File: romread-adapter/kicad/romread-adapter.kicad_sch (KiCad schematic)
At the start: 27 parts

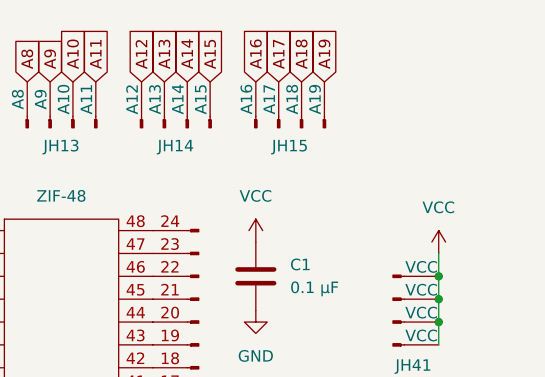
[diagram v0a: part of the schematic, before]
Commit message: romread-adapter sch pcb: Add C2
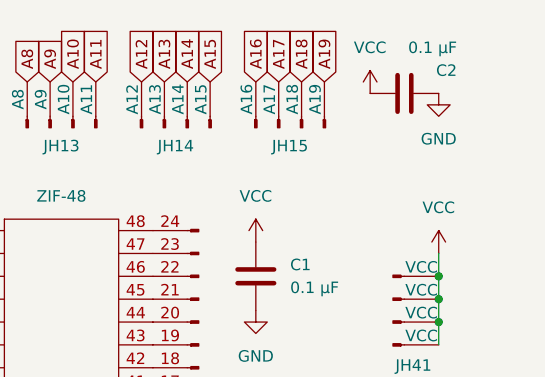
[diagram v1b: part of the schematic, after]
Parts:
- added C2: 0.1 μF, Capacitor_THT:C_Axial_L3.8mm_D2.6mm_P10.00mm_Horizontal, symbol Device:C
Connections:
- net GND: now also C2.2
- net VCC: now also C2.1
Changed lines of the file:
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@@
+	(symbol
+		(lib_id "power:VCC")
+		(at 172.72 49.53 0)
+		(unit 1)
+		(exclude_from_sim no)
+		(in_bom yes)
+		(on_board yes)
+		(dnp no)
+		(fields_autoplaced yes)
+		(property "Reference" "#PWR010"
+			(at 172.72 53.34 0)
+			(effects
+				(font
+					(size 1.27 1.27)
+				)
+				(hide yes)
+			)
+		)
+		(property "Value" "VCC"
+			(at 172.72 44.45 0)
+			(effects
+				(font
+					(size 1.27 1.27)
+				)
+			)
+		)
+		(property "Footprint" ""
+			(at 172.72 49.53 0)
+			(effects
+				(font
+					(size 1.27 1.27)
+				)
+				(hide yes)
+			)
+		)
+		(property "Datasheet" ""
+			(at 172.72 49.53 0)
+			(effects
+				(font
+					(size 1.27 1.27)
+				)
+				(hide yes)
+			)
+		)
+		(property "Description" "Power symbol creates a global label with name \"VCC\""
+			(at 172.72 49.53 0)
+			(effects
+				(font
+					(size 1.27 1.27)
+				)
+				(hide yes)
+			)
+		)
+		(pin "1"
+		)
+		(instances
+			(project ""
+				(path "/65bf6d13-0c24-4e8f-8a57-e3ae2776eac6"
+					(reference "#PWR010")
+					(unit 1)
+				)
+			)
+		)
+	)
+	(symbol
+		(lib_id "power:GND")
+		(at 180.34 49.53 0)
+		(unit 1)
+		(exclude_from_sim no)
+		(in_bom yes)
+		(on_board yes)
+		(dnp no)
+		(fields_autoplaced yes)
+		(property "Reference" "#PWR011"
+			(at 180.34 55.88 0)
+			(effects
+				(font
+					(size 1.27 1.27)
+				)
+				(hide yes)
+			)
+		)
+		(property "Value" "GND"
+			(at 180.34 54.61 0)
+			(effects
+				(font
+					(size 1.27 1.27)
+				)
+			)
+		)
+		(property "Footprint" ""
+			(at 180.34 49.53 0)
+			(effects
+				(font
+					(size 1.27 1.27)
+				)
+				(hide yes)
+			)
+		)
+		(property "Datasheet" ""
+			(at 180.34 49.53 0)
+			(effects
+				(font
+					(size 1.27 1.27)
+				)
+				(hide yes)
+			)
+		)
+		(property "Description" "Power symbol creates a global label with name \"GND\" , ground"
+			(at 180.34 49.53 0)
+			(effects
+				(font
+					(size 1.27 1.27)
+				)
+				(hide yes)
+			)
+		)
+		(pin "1"
+		)
+		(instances
+			(project "romread-adapter"
+				(path "/65bf6d13-0c24-4e8f-8a57-e3ae2776eac6"
+					(reference "#PWR011")
+					(unit 1)
+				)
+			)
+		)
+	)
+	(symbol
+		(lib_id "Device:C")
+		(at 176.53 49.53 90)
+		(unit 1)
+		(exclude_from_sim no)
+		(in_bom yes)
+		(on_board yes)
+		(dnp no)
+		(property "Reference" "C2"
+			(at 182.372 46.99 90)
+			(effects
+				(font
+					(size 1.27 1.27)
+				)
+				(justify left)
+			)
+		)
+		(property "Value" "0.1 μF"
+			(at 182.372 44.45 90)
+			(effects
+				(font
+					(size 1.27 1.27)
+				)
+				(justify left)
+			)
+		)
+		(property "Footprint" "Capacitor_THT:C_Axial_L3.8mm_D2.6mm_P10.00mm_Horizontal"
+			(at 180.34 48.5648 0)
+			(effects
+				(font
+					(size 1.27 1.27)
+				)
+				(hide yes)
+			)
+		)
+		(property "Datasheet" "~"
+			(at 176.53 49.53 0)
+			(effects
+				(font
+					(size 1.27 1.27)
+				)
+				(hide yes)
+			)
+		)
+		(property "Description" "Unpolarized capacitor"
+			(at 176.53 49.53 0)
+			(effects
+				(font
+					(size 1.27 1.27)
+				)
+				(hide yes)
+			)
+		)
+		(pin "2"
+		)
+		(pin "1"
+		)
+		(instances
+			(project "romread-adapter"
+				(path "/65bf6d13-0c24-4e8f-8a57-e3ae2776eac6"
+					(reference "C2")
+					(unit 1)
+				)
+			)
+		)
+	)
 	(symbol
 		(lib_id "power:VCC")
